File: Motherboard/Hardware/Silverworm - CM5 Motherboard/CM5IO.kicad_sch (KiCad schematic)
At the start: 14 parts, among them J11 USB_C_Receptacle_USB2.0

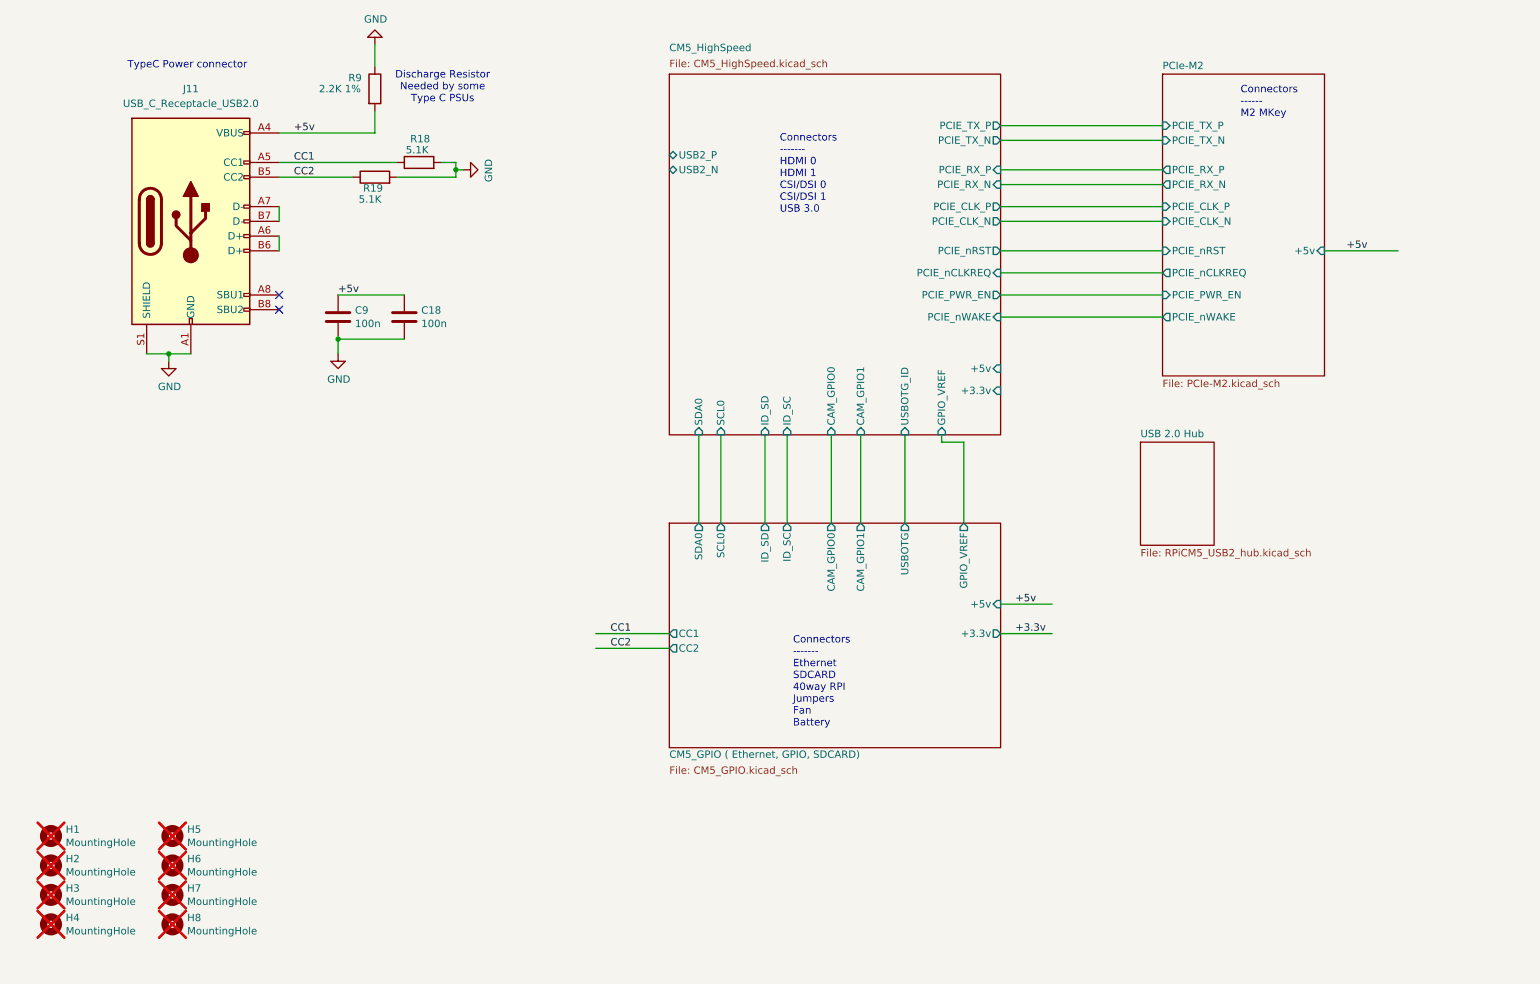
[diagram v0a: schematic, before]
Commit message: Added footprints and board connectors
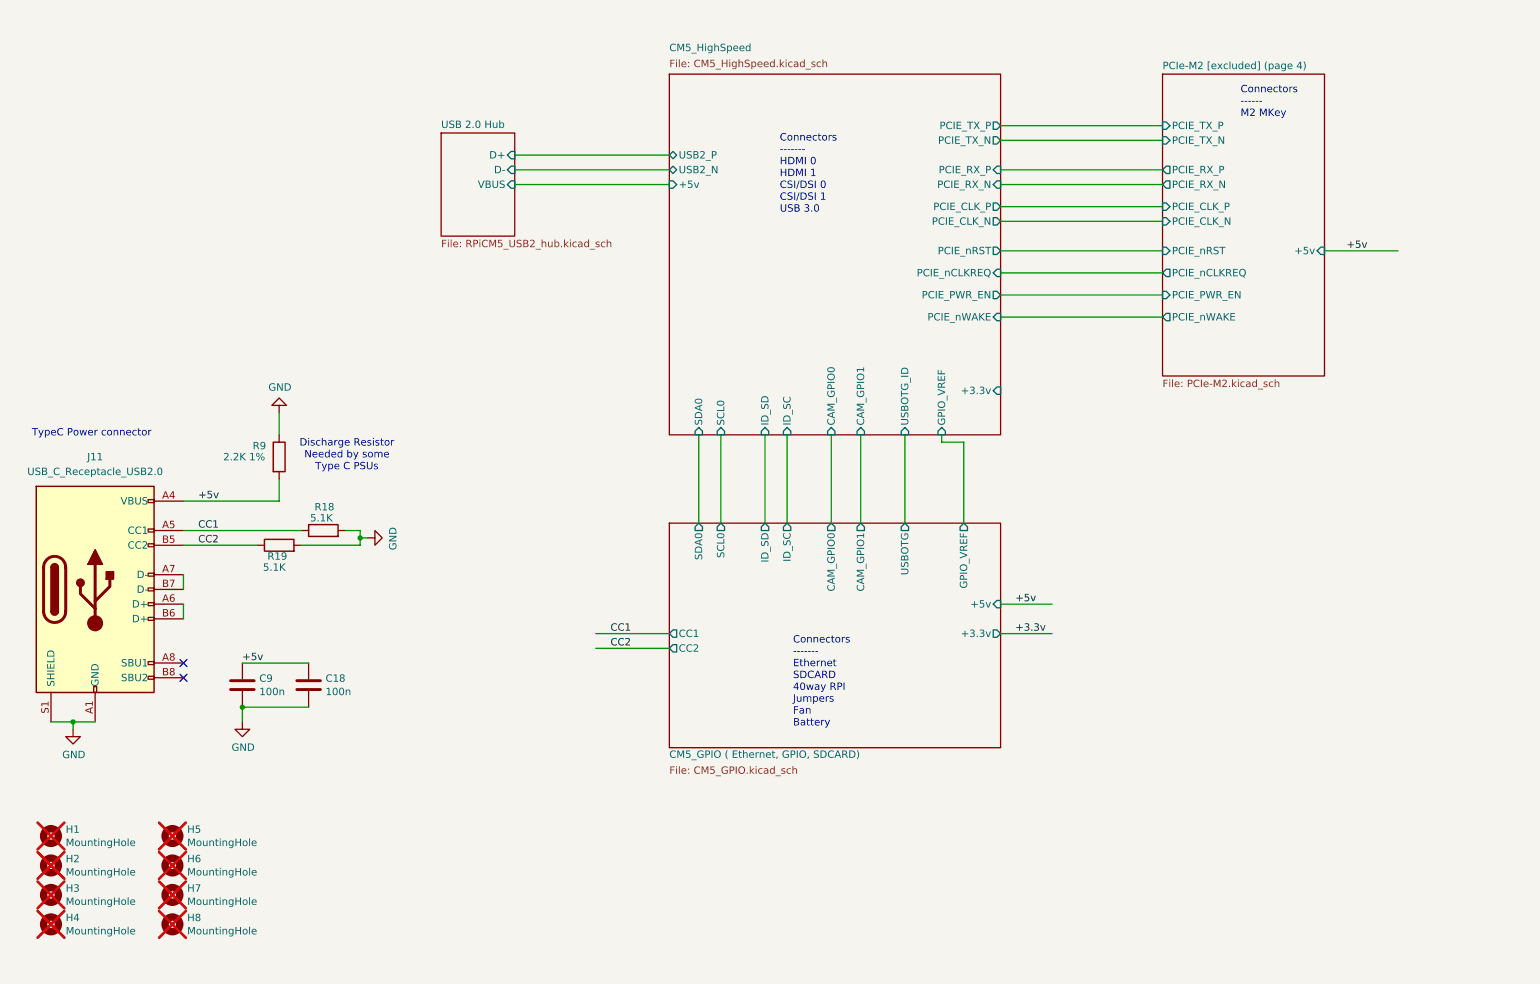
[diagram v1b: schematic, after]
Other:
- sheet PCIe-M2 renamed PCIe-M2 [excluded] (page 4)
- sheet USB 2.0 Hub ports: added D+, D-, VBUS; removed none
- moved on the sheet: C18, C9, J11, R18, R19, R9

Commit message: PCB changes (many)
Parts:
- added 5V_Fan1: 1x2 Pin Header, Connector_PinHeader_2.54mm:PinHeader_1x02_P2.54mm_Vertical, symbol Connector:Conn_01x02_Pin
- renumbered C9 to C1, C18 to C2, J11 to J1, R9 to R1, R19 to R2, R18 to R3
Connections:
- net GND: now also 5V_Fan1.2 (Pin_2)
- net +5v renamed +5V
- net +5V: now also 5V_Fan1.1 (Pin_1)
- no-connect marks 2 -> 3
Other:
- added sheet Power_supply (power_supply.kicad_sch)
- sheet CM5_HighSpeed ports: added none; removed +5v
- sheet USB 2.0 Hub ports: added none; removed VBUS
